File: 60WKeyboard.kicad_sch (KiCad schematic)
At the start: 75 parts, among them IC1 TPD8S300ARUKR, J1 USB4215-03-A_REVA, J2 Conn_02x01_MountingPin, J3 Conn_01x04_Socket, Q1 DMG2301L, U1 PES12-42S-N0024, U3 nRF52840, Y1 ABM11W-32.0000MHZ-7-D1X-T3, Y2 ECS-.327-7-12-TR

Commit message: Finalize V1
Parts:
- removed C25, C26: 10nF, Capacitor_SMD:C_0402_1005Metric, symbol Device:C
- removed R4, R5, R6, R7: 10K, Resistor_SMD:R_0402_1005Metric, symbol Device:R
- removed U1: PES12-42S-N0024, SamacSys_Parts:PES1242SN0024, symbol SamacSys_Parts:PES12-42S-N0024
- added J4: Conn_01x05, symbol Connector_Generic:Conn_01x05
- added SHPHLD: VBUSOUT, TestPoint:TestPoint_Pad_D2.0mm, symbol Connector:TestPoint
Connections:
- net SHPHLD: now also SHPHLD.1
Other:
- note removed: "Rotary Encoder"
- note removed: "check for alternative that fits or drop"
- moved on the sheet: C18, C3, C39, C9, IC1, R10

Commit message: v2 is coming along
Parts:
- removed 3V3: USB_VBUS, TestPoint:TestPoint_Pad_D2.0mm, symbol Connector:TestPoint
- removed C16: 1.5pF, Capacitor_SMD:C_0201_0603Metric, symbol Device:C
- removed C20: 2.2uF, Capacitor_SMD:C_0402_1005Metric, symbol Device:C
- removed C21: 10uF, Capacitor_SMD:C_0603_1608Metric, symbol Device:C
- removed C24: 100nF, Capacitor_SMD:C_0402_1005Metric, symbol Device:C
- removed C3: 0.1uF, Capacitor_SMD:C_0402_1005Metric, symbol Device:C
- removed C39: 1uF, Capacitor_SMD:C_0402_1005Metric, symbol Device:C
- removed C9: 1nF, Capacitor_SMD:C_0402_1005Metric, symbol Device:C
- removed E1: AMCA31-2R450G-S1F-T3, SamacSys_Parts:XDCR_AMCA31-2R450G-S1F-T3, symbol AMCA31-2R450G-S1F-T3:AMCA31-2R450G-S1F-T3
- removed IC1: TPD8S300ARUKR, SamacSys_Parts:QFN40P300X300X80-21N-D, symbol SamacSys_Parts:TPD8S300ARUKR
- removed J1: USB4215-03-A_REVA, SamacSys_Parts:GCT_USB4215-03-A_REVA, symbol USB4215-03-A_REVA:USB4215-03-A_REVA
- removed L5: 2.2uH, Inductor_SMD:L_0805_2012Metric, symbol Device:L
- removed L6: 3.9nH, Inductor_SMD:L_0201_0603Metric, symbol Device:L
- removed R10: 100k, Resistor_SMD:R_0402_1005Metric, symbol Device:R
- removed TP5: VBAT, TestPoint:TestPoint_Pad_D2.0mm, symbol Connector:TestPoint
- added 3V1: USB_VBUS, TestPoint:TestPoint_Pad_D2.0mm, symbol Connector:TestPoint
- added C25, C26: 10uF, Capacitor_SMD:C_0603_1608Metric, symbol Device:C
- added J4: Conn_Coaxial, Connector_Coaxial:U.FL_Hirose_U.FL-R-SMT-1_Vertical, symbol Connector:Conn_Coaxial
- added J5: USB4215-03-A_REVA, SamacSys_Parts:GCT_USB4215-03-A_REVA, symbol USB4215-03-A_REVA:USB4215-03-A_REVA
- added L2: 2.2uH, Inductor_SMD:L_0805_2012Metric, symbol Device:L
- C17: value 10uF -> 100nF; footprint Capacitor_SMD:C_0603_1608Metric -> Capacitor_SMD:C_0402_1005Metric
- C18: value 1nF -> 1uF
- C19: value 1uF -> 2.2uF
- J3: renamed from J4; footprint (none) -> Connector_JST:JST_SH_SM05B-SRSS-TB_1x05-1MP_P1.00mm_Horizontal
- PMIC1: footprint SamacSys_Parts:QFN50P500X500X90-33N -> QFN50P500X500X90-33N
- R1: value 10k -> 250k; footprint Resistor_SMD:R_0402_1005Metric -> Resistor_SMD:R_0805_2012Metric
- R3: value 250k -> 10k; footprint Resistor_SMD:R_0805_2012Metric -> Resistor_SMD:R_0402_1005Metric
- renumbered C31 to C1, C37 to C10, C1 to C11, C38 to C13, C13 to C14, C14 to C15, C15 to C16, C34 to C2, C10 to C20, C7 to C21, C11 to C22, C8 to C24, C4 to C27, C5 to C28, C6 to C29, C33 to C3, C2 to C4, C32 to C5, C35 to C6, C30 to C7, C36 to C8, C29 to C9, D62 to D1, J2 to J1, J3 to J2, L3 to L1, L4 to L3, R9 to R4, SHPHLD to SHPHLD1, U3 to U1
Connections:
- net +3V3: now also R2.2, R3.2, 3V1.1, C26.1, L2.1; no longer R1.1, R2.1
- net +5V: now also C25.1
- net +BATT: now also C19.2
- net COL_0: now also U1.A8 (AIN7/P0.31); no longer U1.AC21 (P0.25)
- net COL_1: now also U1.A10 (AIN5/P0.29); no longer U1.AC19 (P0.23)
- net COL_9: no longer U1.AD12 (P0.17)
- net C_CC1: now also J5.A5 (CC1)
- net C_CC2: now also J5.B5 (CC2)
- net C_VBUS: now also J3.1 (Pin_1), J5.A4_B9 (VBUS_A), J5.B4_A9 (VBUS_B)
- net GND: now also C19.1, J3.4 (Pin_4), R1.1, C25.2, C26.2, J4.2 (Ext), J5.A1_B12 (GND_A), J5.B1_A12 (GND_B), J5.SH1 (SHIELD), J5.SH2 (SHIELD__1), J5.SH3 (SHIELD__2), J5.SH4 (SHIELD__3); no longer C19.2, R3.2
- net RESET: now also U1.AD12 (P0.17)
- net RF: now also L3.2, J4.1 (In)
- net SBU1: now also J5.A8 (SBU1)
- net SBU2: now also J5.B8 (SBU2)
- net SCL: now also R2.1; no longer R1.2
- net SDA: now also R3.1; no longer R2.2
- net SHPHLD: no longer PMIC1.15 (SHPHLD)
- net USB_DN: now also J3.2 (Pin_2), J5.A7 (DN1), J5.B7 (DN2)
- net USB_DP: now also J3.3 (Pin_3), J5.A6 (DP1), J5.B6 (DP2)
- net VBUS: now also C18.1; no longer C19.1
- net PWR_SW: now reaches J3.5 (Pin_5)
- net CC1: no longer names the net of PMIC1.23 (CC1)
- net CC2: no longer names the net of PMIC1.24 (CC2)
- net CC2: no longer C18.1
- net SW2: no longer names the net of PMIC1.5 (SW2)
- net SW2: now also L2.2
- net VSET2: no longer names the net of PMIC1.16 (VSET2)
- net VSET2: now also R1.2; no longer R3.1
- no-connect marks 33 -> 31
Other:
- note removed: "Ground to PVSS2"
- note removed: "Net Tie"
- moved on the sheet: C20, C22, C27, C28, C29, J3, L1, L3, PMIC1, SHPHLD1

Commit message: more v2 work
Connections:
- net COL_10: no longer U1.AD16 (P0.20)
- net COL_2: now also U1.A14 (P1.15); no longer U1.AC17 (P0.21)
- net COL_3: now also U1.A12 (AIN0/P0.02); no longer U1.AC15 (P0.19)
- net COL_4: now also U1.A20 (P1.10); no longer U1.AC11 (P0.16)
- net COL_5: now also U1.B19 (P1.11); no longer U1.AC9 (P0.14)
- net COL_6: now also U1.U1 (TRACEDATA1/P0.12); no longer U1.G1 (P0.26)
- net COL_7: now also U1.N1 (P0.08); no longer U1.AD8 (P0.13)
- net COL_8: now also U1.R1 (TRACEDATA3/P1.09); no longer U1.AD10 (P0.15)
- net ROW_0: no longer U1.U1 (TRACEDATA1/P0.12)
- net ROW_1: no longer U1.N1 (P0.08)
- net ROW_2: no longer U1.M2 (TRACECLK/P0.07)
- net ROW_3: now also U1.AD10 (P0.15); no longer U1.R1 (TRACEDATA3/P1.09)
- net ROW_4: now also U1.AD8 (P0.13); no longer U1.T2 (TRACEDATA2/P0.11)
- net SCL: now also U1.G1 (P0.26); no longer U1.K2 (AIN3/P0.05)
- no-connect marks 31 -> 36

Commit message: v2 - init done, much fixing to go
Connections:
- net COL_0: now also U1.A10 (AIN5/P0.29); no longer U1.A8 (AIN7/P0.31)
- net COL_1: now also U1.A8 (AIN7/P0.31); no longer U1.A10 (AIN5/P0.29)
- net COL_10: now also U1.U24 (P1.04)
- net COL_11: now also U1.W24 (P1.02); no longer U1.AD18 (P0.22)
- net COL_12: now also U1.J24 (NFC2/P0.10); no longer U1.AD20 (P0.24)
- net COL_13: now also U1.R24 (P1.06); no longer U1.AD22 (TRACEDATA0/P1.00)
- net COL_9: now also U1.AD22 (TRACEDATA0/P1.00)
- net PWR_SW: now also U1.L24 (NFC1/P0.09)
- net ROW_0: now also U1.AD20 (P0.24)
- net ROW_1: now also U1.AD18 (P0.22)
- net ROW_2: now also U1.AD16 (P0.20)
- net SHPHLD: now also PMIC1.15 (SHPHLD)
- no-connect marks 36 -> 30
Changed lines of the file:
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@@
 	)
 	(no_connect
-		(at 158.75 254)
-	)
-	(no_connect
 		(at 158.75 231.14)
 	)
@@
 	)
 	(no_connect
-		(at 158.75 187.96)
-	)
-	(no_connect
-		(at 158.75 259.08)
-	)
-	(no_connect
-		(at 158.75 248.92)
-	)
-	(no_connect
 		(at 284.48 541.02)
 	)
@@
 	)
 	(no_connect
-		(at 158.75 210.82)
-	)
-	(no_connect
-		(at 158.75 185.42)
-	)
-	(no_connect
 		(at 284.48 491.49)
 	)
@@
 	(wire
 		(pts
+			(xy 158.75 248.92) (xy 161.29 248.92)
+		)
+		(stroke
+			(width 0)
+			(type default)
+		)
+	)
+	(wire
+		(pts
 			(xy 464.82 212.09) (xy 467.36 212.09)
 		)
@@
 	(wire
 		(pts
+			(xy 158.75 185.42) (xy 161.29 185.42)
+		)
+		(stroke
+			(width 0)
+			(type default)
+		)
+	)
+	(wire
+		(pts
 			(xy 161.29 243.84) (xy 158.75 243.84)
 		)
@@
 	(wire
 		(pts
+			(xy 281.94 553.72) (xy 284.48 553.72)
+		)
+		(stroke
+			(width 0)
+			(type default)
+		)
+	)
+	(wire
+		(pts
 			(xy 152.4 125.73) (xy 152.4 124.46)
 		)
@@
 	(wire
 		(pts
+			(xy 158.75 254) (xy 161.29 254)
+		)
+		(stroke
+			(width 0)
+			(type default)
+		)
+	)
+	(wire
+		(pts
 			(xy 407.67 160.02) (xy 407.67 161.29)
 		)
@@
 	(wire
 		(pts
+			(xy 158.75 187.96) (xy 161.29 187.96)
+		)
+		(stroke
+			(width 0)
+			(type default)
+		)
+	)
+	(wire
+		(pts
 			(xy 558.8 312.42) (xy 556.26 312.42)
 		)
@@
 	(wire
 		(pts
+			(xy 158.75 259.08) (xy 161.29 259.08)
+		)
+		(stroke
+			(width 0)
+			(type default)
+		)
+	)
+	(wire
+		(pts
 			(xy 368.3 500.38) (xy 379.73 500.38)
 		)
@@
 	(wire
 		(pts
+			(xy 158.75 210.82) (xy 161.29 210.82)
+		)
+		(stroke
+			(width 0)
+			(type default)
+		)
+	)
+	(wire
+		(pts
 			(xy 388.62 119.38) (xy 391.16 119.38)
 		)
@@
 		)
 	)
+	(label "COL_11"
+		(at 161.29 248.92 0)
+		(effects
+			(font
+				(size 1.27 1.27)
+			)
+			(justify left bottom)
+		)
+	)
 	(label "DEC 1"
 		(at 105.41 152.4 90)
@@
 		)
 	)
+	(label "COL_10"
+		(at 161.29 254 0)
+		(effects
+			(font
+				(size 1.27 1.27)
+			)
+			(justify left bottom)
+		)
+	)
 	(label "USB_DN"
 		(at 161.29 287.02 0)
@@
 		)
 	)
+	(label "ROW_2"
+		(at 161.29 210.82 0)
+		(effects
+			(font
+				(size 1.27 1.27)
+			)
+			(justify left bottom)
+		)
+	)
 	(label "COL_5"
 		(at 482.6 120.65 180)
@@
 		)
 	)
+	(label "COL_0"
+		(at 161.29 233.68 0)
+		(effects
+			(font
+				(size 1.27 1.27)
+			)
+			(justify left bottom)
+		)
+	)
 	(label "XC1"
 		(at 218.44 237.49 180)
@@
 		)
 	)
-	(label "COL_1"
-		(at 161.29 233.68 0)
+	(label "SHPHLD"
+		(at 281.94 553.72 180)
 		(effects
 			(font
 				(size 1.27 1.27)
 			)
-			(justify left bottom)
+			(justify right bottom)
 		)
 	)
@@
 		)
 	)
-	(label "SCL"
-		(at 266.7 558.8 180)
+	(label "COL_12"
+		(at 161.29 187.96 0)
 		(effects
 			(font
 				(size 1.27 1.27)
 			)
-			(justify right bottom)
+			(justify left bottom)
 		)
 	)
-	(label "ROW_0"
-		(at 508 107.95 0)
+	(label "SCL"
+		(at 266.7 558.8 180)
 		(effects
 			(font
 				(size 1.27 1.27)
 			)
-			(justify left bottom)
+			(justify right bottom)
 		)
 	)
-	(label "COL_0"
-		(at 161.29 238.76 0)
+	(label "ROW_0"
+		(at 508 107.95 0)
 		(effects
 			(font
@@
 		)
 	)
-	(label "ROW_1"
-		(at 181.61 193.04 0)
+	(label "PWR_SW"
+		(at 161.29 185.42 0)
 		(effects
 			(font
@@
 		)
 	)
-	(label "COL_13"
-		(at 161.29 243.84 0)
+	(label "ROW_0"
+		(at 161.29 220.98 0)
 		(effects
 			(font
@@
 		)
 	)
-	(label "COL_12"
-		(at 161.29 220.98 0)
+	(label "ROW_1"
+		(at 161.29 215.9 0)
 		(effects
 			(font
@@
 		)
 	)
-	(label "ROW_0"
-		(at 186.69 182.88 0)
-		(effects
-			(font
-				(size 1.27 1.27)
-			)
-			(justify left bottom)
-		)
-	)
 	(label "COL_8"
 		(at 161.29 266.7 0)
@@
 		)
 	)
+	(label "COL_1"
+		(at 161.29 238.76 0)
+		(effects
+			(font
+				(size 1.27 1.27)
+			)
+			(justify left bottom)
+		)
+	)
 	(label "C_VBUS"
 		(at 518.16 304.8 180)
@@
 		)
 	)
-	(label "COL_10"
-		(at 181.61 209.55 0)
-		(effects
-			(font
-				(size 1.27 1.27)
-			)
-			(justify left bottom)
-		)
-	)
-	(label "ROW_2"
-		(at 184.15 267.97 0)
+	(label "COL_9"
+		(at 161.29 243.84 0)
 		(effects
 			(font
@@
 		)
 	)
-	(label "PWR_SW"
-		(at 182.88 234.95 180)
+	(label "COL_13"
+		(at 161.29 259.08 0)
 		(effects
 			(font
 				(size 1.27 1.27)
 			)
-			(justify right bottom)
+			(justify left bottom)
 		)
 	)
@@
 		)
 	)
-	(label "COL_9"
-		(at 186.69 198.12 0)
-		(effects
-			(font
-				(size 1.27 1.27)
-			)
-			(justify left bottom)
-		)
-	)
 	(label "SBU1"
 		(at 518.16 317.5 180)
@@
 		(effects
 			(font
-				(size 1.27 1.27)
-			)
-			(justify left bottom)
-		)
-	)
-	(label "COL_11"
-		(at 161.29 215.9 0)
-		(effects
-			(font

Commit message: v2 - doneish
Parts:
- removed J3: Conn_01x05, Connector_JST:JST_SH_SM05B-SRSS-TB_1x05-1MP_P1.00mm_Horizontal, symbol Connector_Generic:Conn_01x05
- removed J5: USB4215-03-A_REVA, SamacSys_Parts:GCT_USB4215-03-A_REVA, symbol USB4215-03-A_REVA:USB4215-03-A_REVA
- added C32: 100nF, Capacitor_SMD:C_0402_1005Metric, symbol Device:C
- added J4: Conn_01x05_MountingPin, Connector_JST:JST_SH_SM05B-SRSS-TB_1x05-1MP_P1.00mm_Horizontal, symbol Connector_Generic_MountingPin:Conn_01x05_MountingPin
- added R6: 10k, Resistor_SMD:R_0402_1005Metric, symbol Device:R
- PMIC1: footprint QFN50P500X500X90-33N -> SamacSys_Parts:QFN50P500X500X90-33N
- renumbered C17 to C14, C18 to C15, C19 to C16, C14 to C17, C15 to C18, C16 to C19, C23 to C20, C25 to C21, C26 to C22, C27 to C23, C28 to C24, C29 to C25, C20 to C26, C21 to C27, C22 to C28, C24 to C29, J4 to J5, L2 to L1, L1 to L2
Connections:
- net +3V3: now also R6.1
- net C_VBUS: now also J4.1 (Pin_1)
- net GND: now also C32.1, J4.4 (Pin_4), J4.MP (MountPin)
- net PWR_SW: now also C32.2, J4.5 (Pin_5), R6.2
- net USB_DN: now also J4.2 (Pin_2)
- net USB_DP: now also J4.3 (Pin_3)
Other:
- moved on the sheet: 3V1, 5V1, C1, C10, C11, C12, C13, C14, C15, C16, C17, C18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

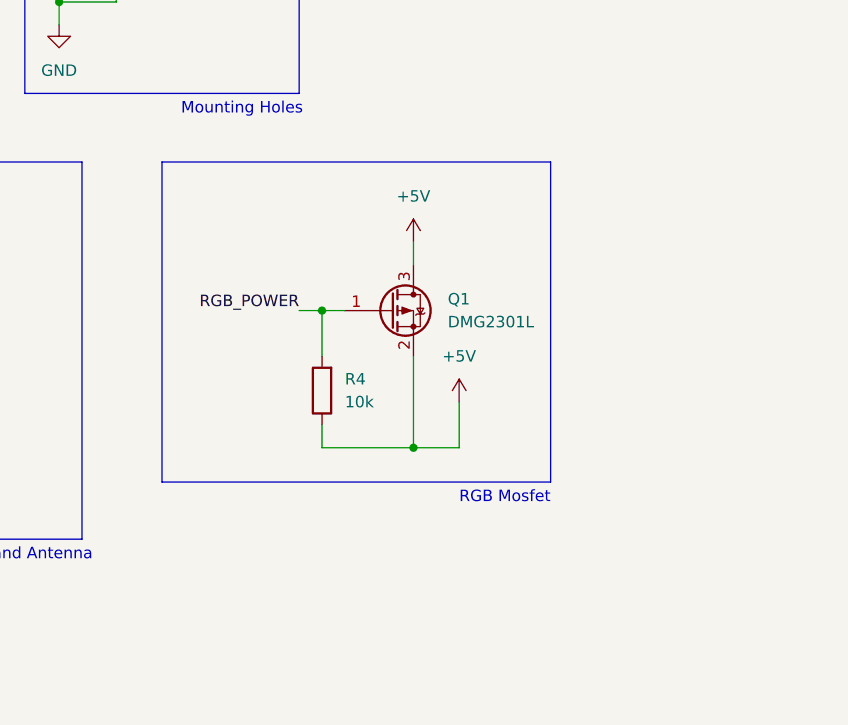
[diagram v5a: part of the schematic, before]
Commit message: fixed the p channel mosfet not working
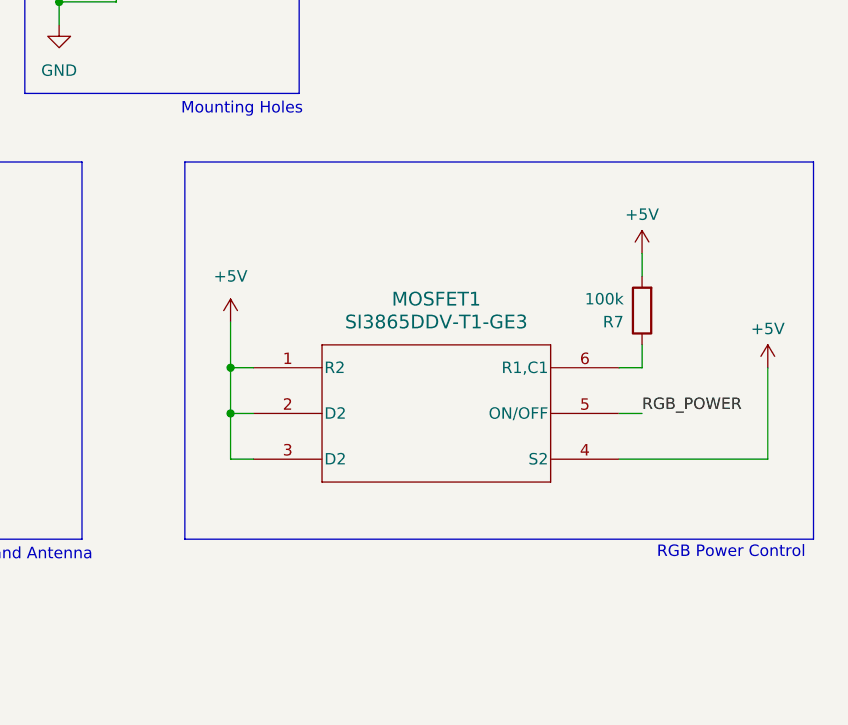
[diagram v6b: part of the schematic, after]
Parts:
- removed Q1: DMG2301L, Package_TO_SOT_SMD:SOT-23, symbol Transistor_FET:DMG2301L
- removed R4: 10k, Resistor_SMD:R_0402_1005Metric, symbol Device:R
- added MOSFET1: SI3865DDV-T1-GE3, SamacSys_Parts:TSOP6_MO-193C_VIS, symbol SI3865DDV:SI3865DDV-T1-GE3
- added R7: 100k, Resistor_SMD:R_0402_1005Metric, symbol Device:R
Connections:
- net +5V: now also MOSFET1.1 (R2), MOSFET1.2 (D2), MOSFET1.3 (D2), MOSFET1.4 (S2), R7.2
- net RGB_POWER: now also MOSFET1.5 (ON/OFF)
- new net: MOSFET1.6 (R1,C1), R7.1
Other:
- note added: "RGB Power Control"
- note removed: "RGB Mosfet"
